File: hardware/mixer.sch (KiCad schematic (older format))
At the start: 31 parts, among them U26 5400BL15B050E, U27 5400BL15B050E, U28 5400BL15B050E, U29 ADL5802

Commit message: Current working version.
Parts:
- C107, C162: footprint fmcw3:C_0805b -> Capacitor_SMD:C_0805_2012Metric; symbol C -> Device:C
- C108, C115, C116, C117, C118, C119, C120, C121, C122, C123: footprint fmcw3:C_0402b -> Capacitor_SMD:C_0402_1005Metric; symbol C -> Device:C
- C109, C110, C111, C112, C113, C114: value 10p -> 3p; footprint fmcw3:C_0402b -> Capacitor_SMD:C_0402_1005Metric; symbol C -> Device:C
- F1, F2: symbol Via -> fmcw3-rescue:Via
- FB13: symbol FILTER -> Device:Ferrite_Bead
- R49, R50, R51, R52, R53, R54: symbol R -> Device:R
- U26, U27, U28: symbol 5400BL15B050E -> fmcw3-rescue:5400BL15B050E
- U29: footprint Housings_DFN_QFN:QFN-24-1EP_4x4mm_Pitch0.5mm -> Package_DFN_QFN:QFN-24-1EP_4x4mm_P0.5mm_EP2.6x2.6mm; symbol ADL5802 -> fmcw3-rescue:ADL5802; manf# (none) -> ADL5802ACPZ-R7
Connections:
- wire segments 91 -> 122

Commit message: Dropped the 3 from the end of the project name.
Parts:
- F1, F2: footprint fmcw3:RF_via -> fmcw:RF_via; symbol fmcw3-rescue:Via -> fmcw-rescue:Via-fmcw3-rescue
- FB13: footprint fmcw3:C_0603b -> fmcw:C_0603b
- R49, R50, R51, R52, R53, R54: footprint fmcw3:R_0402b -> fmcw:R_0402b
- U26, U27, U28: footprint fmcw3:5400BL15B050E -> fmcw:5400BL15B050E; symbol fmcw3-rescue:5400BL15B050E -> fmcw-rescue:5400BL15B050E-fmcw3-rescue
- U29: symbol fmcw3-rescue:ADL5802 -> fmcw-rescue:ADL5802-fmcw3-rescue
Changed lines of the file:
@@
 EESchema Schematic File Version 4
-LIBS:fmcw3-cache
+LIBS:fmcw-cache
 EELAYER 26 0
 EELAYER END
@@
 $EndComp
 $Comp
-L fmcw3-rescue:5400BL15B050E U?
+L fmcw-rescue:5400BL15B050E-fmcw3-rescue U?
 U 1 1 593ACD34
 P 2650 4550
@@
 F 0 "U26" H 2900 4800 60  0000 C CNN
 F 1 "5400BL15B050E" H 2750 5250 60  0000 C CNN
-F 2 "fmcw3:5400BL15B050E" H 2650 4550 60  0001 C CNN
-F 3 "https://www.johansontechnology.com/datasheets/baluns/Balun_5400BL15B050.pdf" H 2650 4550 60  0001 C CNN
+F 2 "fmcw:5400BL15B050E" H 2650 4550 60  0001 C CNN
+F 3 "https://www.johansontechnology.com/datasheets/5400BL15B050/5400BL15B050.pdf" H 2650 4550 60  0001 C CNN
 	1    2650 4550
 	1    0    0    -1
@@
 F 0 "R51" H 8330 3254 50  0000 R CNN
 F 1 "49.9" H 8330 3345 50  0000 R CNN
-F 2 "fmcw3:R_0402b" V 8330 3300 30  0001 C CNN
+F 2 "fmcw:R_0402b" V 8330 3300 30  0001 C CNN
 F 3 "" H 8400 3300 30  0000 C CNN
 	1    8400 3300
@@
 F 0 "R52" H 8330 3654 50  0000 R CNN
 F 1 "49.9" H 8330 3745 50  0000 R CNN
-F 2 "fmcw3:R_0402b" V 8330 3700 30  0001 C CNN
+F 2 "fmcw:R_0402b" V 8330 3700 30  0001 C CNN
 F 3 "" H 8400 3700 30  0000 C CNN
 	1    8400 3700
@@
 5V
 $Comp
-L fmcw3-rescue:ADL5802 U?
+L fmcw-rescue:ADL5802-fmcw3-rescue U?
 U 1 1 5942E974
 P 4650 4150
@@
 $EndComp
 $Comp
-L fmcw3-rescue:5400BL15B050E U27
+L fmcw-rescue:5400BL15B050E-fmcw3-rescue U27
 U 1 1 5942FD33
 P 2650 5500
@@
 F 0 "U27" H 2900 5750 60  0000 C CNN
 F 1 "5400BL15B050E" H 2750 6200 60  0000 C CNN
-F 2 "fmcw3:5400BL15B050E" H 2650 5500 60  0001 C CNN
+F 2 "fmcw:5400BL15B050E" H 2650 5500 60  0001 C CNN
 F 3 "" H 2650 5500 60  0000 C CNN
 	1    2650 5500
@@
 RF1
 $Comp
-L fmcw3-rescue:5400BL15B050E U28
+L fmcw-rescue:5400BL15B050E-fmcw3-rescue U28
 U 1 1 59430048
 P 2650 6500
@@
 F 0 "U28" H 2900 6750 60  0000 C CNN
 F 1 "5400BL15B050E" H 2750 7200 60  0000 C CNN
-F 2 "fmcw3:5400BL15B050E" H 2650 6500 60  0001 C CNN
+F 2 "fmcw:5400BL15B050E" H 2650 6500 60  0001 C CNN
 F 3 "" H 2650 6500 60  0000 C CNN
 	1    2650 6500
@@
 F 0 "R53" H 8330 4854 50  0000 R CNN
 F 1 "49.9" H 8330 4945 50  0000 R CNN
-F 2 "fmcw3:R_0402b" V 8330 4900 30  0001 C CNN
+F 2 "fmcw:R_0402b" V 8330 4900 30  0001 C CNN
 F 3 "" H 8400 4900 30  0000 C CNN
 	1    8400 4900
@@
 F 0 "R54" H 8330 5254 50  0000 R CNN
 F 1 "49.9" H 8330 5345 50  0000 R CNN
-F 2 "fmcw3:R_0402b" V 8330 5300 30  0001 C CNN
+F 2 "fmcw:R_0402b" V 8330 5300 30  0001 C CNN
 F 3 "" H 8400 5300 30  0000 C CNN
 	1    8400 5300
@@
 F 0 "R50" V 7030 5350 50  0000 C CNN
 F 1 "DNP" V 6950 5350 50  0000 C CNN
-F 2 "fmcw3:R_0402b" V 6880 5350 30  0001 C CNN
+F 2 "fmcw:R_0402b" V 6880 5350 30  0001 C CNN
 F 3 "" H 6950 5350 30  0000 C CNN
 	1    6950 5350
@@
 F 0 "R49" V 7030 4950 50  0000 C CNN
 F 1 "2k" V 6950 4950 50  0000 C CNN
-F 2 "fmcw3:R_0402b" V 6880 4950 30  0001 C CNN
+F 2 "fmcw:R_0402b" V 6880 4950 30  0001 C CNN
 F 3 "" H 6950 4950 30  0000 C CNN
 	1    6950 4950
@@
 F 0 "FB13" V 3600 2050 50  0000 C CNN
 F 1 "BLM18PG181SN1D" V 3500 2200 50  0000 C CNN
-F 2 "fmcw3:C_0603b" H 3650 2200 60  0001 C CNN
+F 2 "fmcw:C_0603b" H 3650 2200 60  0001 C CNN
 F 3 "" H 3650 2200 60  0000 C CNN
 	1    3650 2200
@@
 Connection ~ 5700 2450
 $Comp
-L fmcw3-rescue:Via F1
+L fmcw-rescue:Via-fmcw3-rescue F1
 U 1 1 597038AD
 P 1150 4050
 F 0 "F1" H 1068 4297 60  0000 C CNN
 F 1 "Via" H 1068 4191 60  0000 C CNN
-F 2 "fmcw3:RF_via" H 1150 4050 60  0001 C CNN
+F 2 "fmcw:RF_via" H 1150 4050 60  0001 C CNN
 F 3 "" H 1150 4050 60  0001 C CNN
 	1    1150 4050
@@
 $EndComp
 $Comp
-L fmcw3-rescue:Via F2
+L fmcw-rescue:Via-fmcw3-rescue F2
 U 1 1 5970394E
 P 1900 4050
 F 0 "F2" H 1819 4297 60  0000 C CNN
 F 1 "Via" H 1819 4191 60  0000 C CNN
-F 2 "fmcw3:RF_via" H 1900 4050 60  0001 C CNN
+F 2 "fmcw:RF_via" H 1900 4050 60  0001 C CNN
 F 3 "" H 1900 4050 60  0001 C CNN
 	1    1900 4050

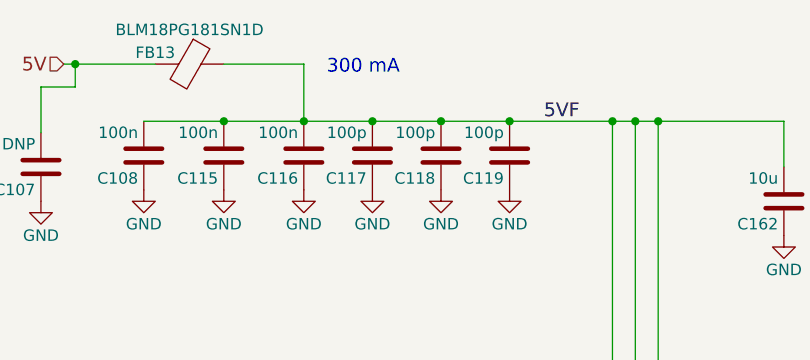
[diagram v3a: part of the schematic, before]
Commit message: Adjusted power supply for new power amplifier.
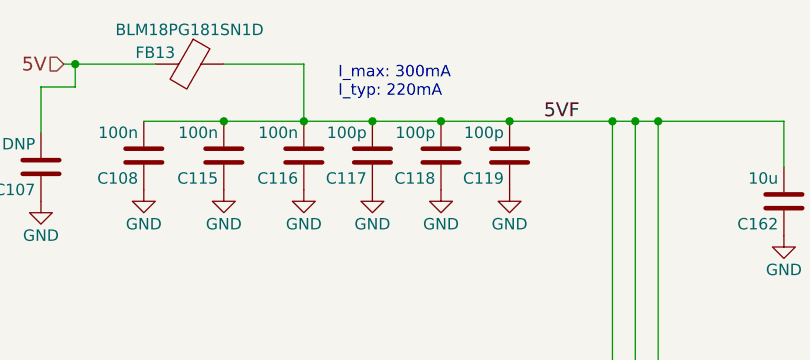
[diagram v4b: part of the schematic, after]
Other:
- note added: "I_max: 300mA\nI_typ: 220mA"
- note removed: "300 mA"
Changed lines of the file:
@@
 EESchema Schematic File Version 4
 LIBS:fmcw-cache
-EELAYER 29 0
+EELAYER 26 0
 EELAYER END
 $Descr A4 11693 8268
@@
 Text Label 6950 4750 0    60   ~ 0
 5VF
-Text Notes 4250 2250 0    60   ~ 0
-300 mA
+Text Notes 4300 2350 0    50   ~ 0
+I_max: 300mA\nI_typ: 220mA
 $Comp
 L Device:Ferrite_Bead FB13

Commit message: Documentation for TPS5420D buck converter.
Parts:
- C162: MFN (none) -> 885012107014
- U29: MFN (none) -> ADL5802ACPZ-R7; manf# ADL5802ACPZ-R7 -> (none)
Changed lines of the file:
@@
 F 2 "Package_DFN_QFN:QFN-24-1EP_4x4mm_P0.5mm_EP2.6x2.6mm" H 4650 4150 60  0001 C CNN
 F 3 "http://www.analog.com/media/en/technical-documentation/data-sheets/ADL5802.pdf" H 4650 4150 60  0001 C CNN
-F 4 "ADL5802ACPZ-R7" H 4650 4150 50  0001 C CNN "manf#"
+F 4 "" H 4650 4150 50  0001 C CNN "manf#"
+F 5 "ADL5802ACPZ-R7" H 0   0   50  0001 C CNN "MFN"
 	1    4650 4150
 	1    0    0    -1
@@
 F 2 "Capacitor_SMD:C_0805_2012Metric" H 6288 2650 30  0001 C CNN
 F 3 "" H 6250 2800 60  0000 C CNN
+F 4 "885012107014" H 0   0   50  0001 C CNN "MFN"
 	1    6250 2800
 	-1   0    0    1

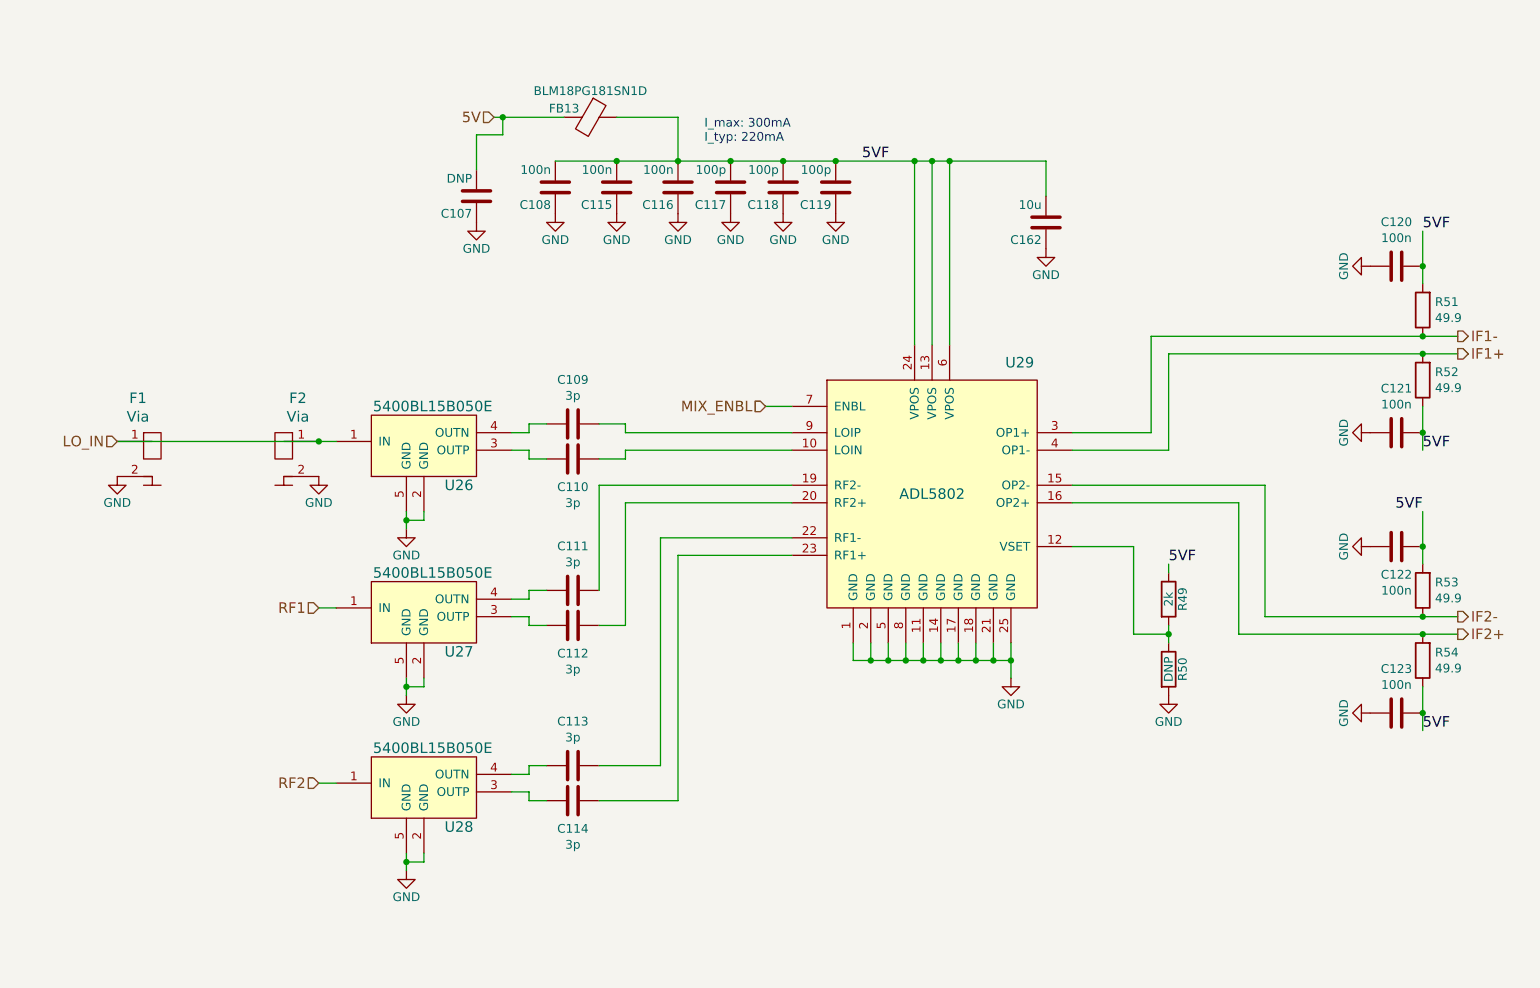
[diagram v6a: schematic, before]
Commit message: Added MFNs to components.
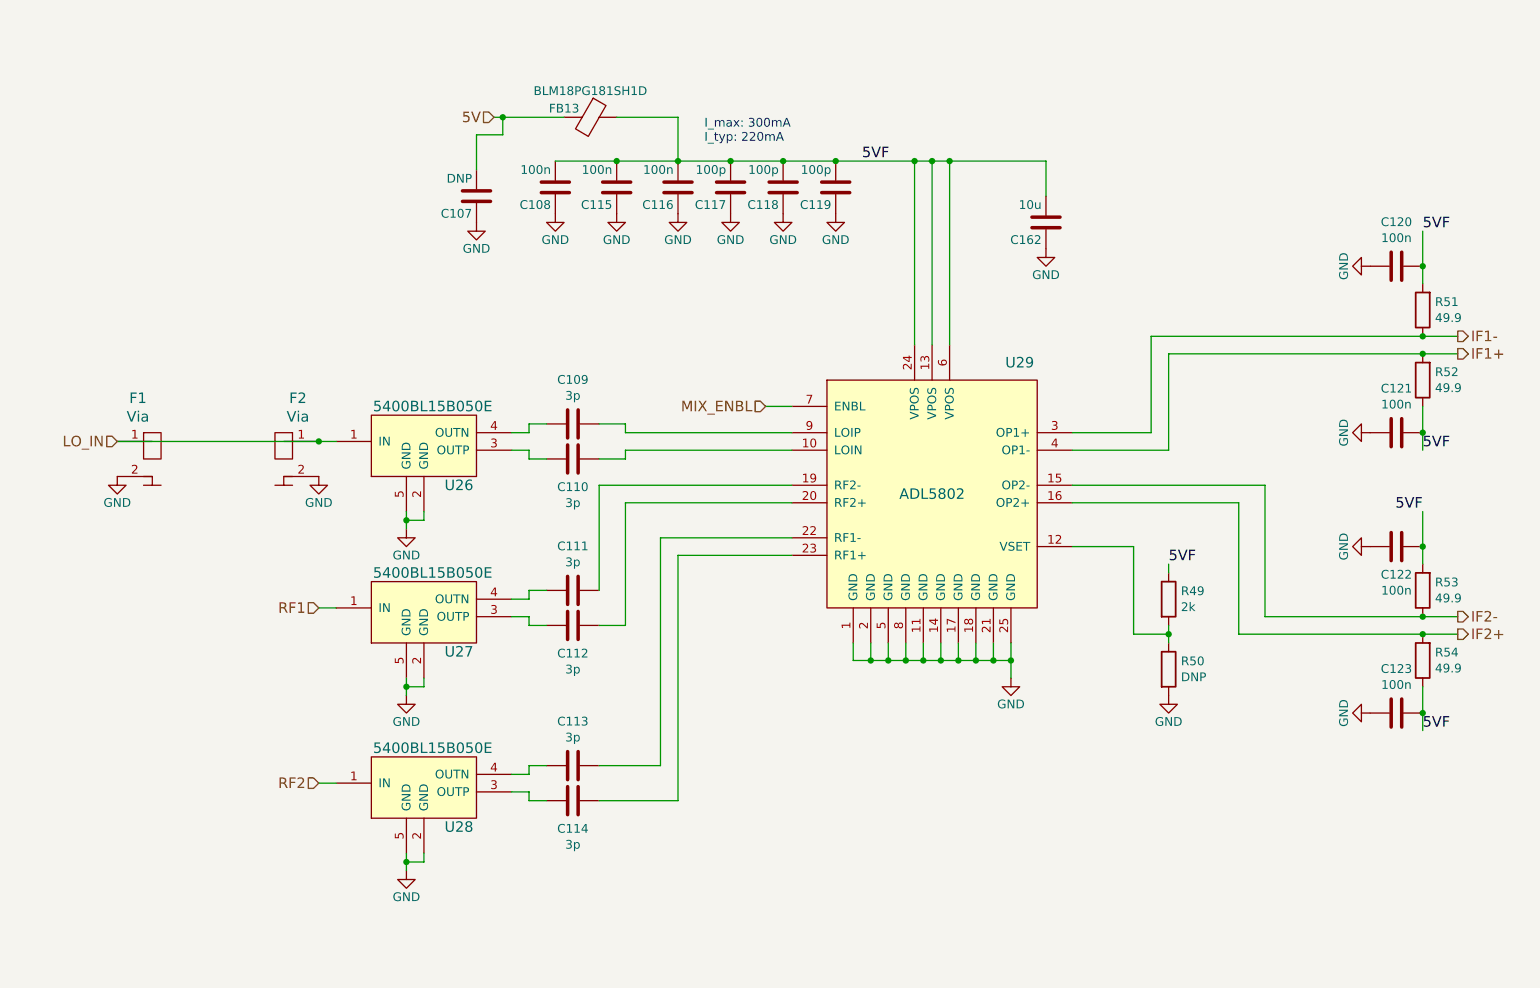
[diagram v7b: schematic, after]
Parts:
- C108, C115, C116, C120, C121, C122, C123: MFN (none) -> CL05B104KO5NNNC
- C109, C110, C111, C112, C113, C114: MFN (none) -> 500R07S3R0BV4T
- C117, C118, C119: MFN (none) -> UMK105CG101JVHF
- C162: MFN 885012107014 -> CL21B106KQQNNNE
- FB13: value BLM18PG181SN1D -> BLM18PG181SH1D; footprint fmcw:C_0603b -> Inductor_SMD:L_0603_1608Metric; MFN (none) -> BLM18PG181SH1D
- R49: footprint fmcw:R_0402b -> Resistor_SMD:R_0402_1005Metric; MFN (none) -> ERJ-2RKF2001X
- R50: footprint fmcw:R_0402b -> Resistor_SMD:R_0402_1005Metric
- R51, R52, R53, R54: footprint fmcw:R_0402b -> Resistor_SMD:R_0402_1005Metric; MFN (none) -> ERJ-2RKF49R9X
- U26, U27, U28: MFN (none) -> 5400BL15B050E
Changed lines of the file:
@@
 F 2 "fmcw:5400BL15B050E" H 2650 4550 60  0001 C CNN
 F 3 "https://www.johansontechnology.com/datasheets/5400BL15B050/5400BL15B050.pdf" H 2650 4550 60  0001 C CNN
+F 4 "5400BL15B050E" H 0   0   50  0001 C CNN "MFN"
 	1    2650 4550
 	1    0    0    -1
@@
 F 2 "Capacitor_SMD:C_0402_1005Metric" H 3588 3800 30  0001 C CNN
 F 3 "" H 3550 3950 60  0000 C CNN
+F 4 " 500R07S3R0BV4T" H 0   0   50  0001 C CNN "MFN"
 	1    3550 3950
 	0    1    1    0
@@
 F 2 "Capacitor_SMD:C_0402_1005Metric" H 3588 4000 30  0001 C CNN
 F 3 "" H 3550 4150 60  0000 C CNN
+F 4 " 500R07S3R0BV4T" H 0   0   50  0001 C CNN "MFN"
 	1    3550 4150
 	0    1    1    0
@@
 F 2 "Capacitor_SMD:C_0402_1005Metric" H 4488 2450 30  0001 C CNN
 F 3 "" H 4450 2600 60  0000 C CNN
+F 4 "UMK105CG101JVHF" H 0   0   50  0001 C CNN "MFN"
 	1    4450 2600
 	-1   0    0    1
@@
 F 2 "Capacitor_SMD:C_0402_1005Metric" H 4188 2450 30  0001 C CNN
 F 3 "" H 4150 2600 60  0000 C CNN
+F 4 "CL05B104KO5NNNC" H 0   0   50  0001 C CNN "MFN"
 	1    4150 2600
 	-1   0    0    1
@@
 F 0 "R51" H 8330 3254 50  0000 R CNN
 F 1 "49.9" H 8330 3345 50  0000 R CNN
-F 2 "fmcw:R_0402b" V 8330 3300 30  0001 C CNN
+F 2 "Resistor_SMD:R_0402_1005Metric" V 8330 3300 30  0001 C CNN
 F 3 "" H 8400 3300 30  0000 C CNN
+F 4 "ERJ-2RKF49R9X" H 0   0   50  0001 C CNN "MFN"
 	1    8400 3300
 	-1   0    0    1
@@
 F 0 "R52" H 8330 3654 50  0000 R CNN
 F 1 "49.9" H 8330 3745 50  0000 R CNN
-F 2 "fmcw:R_0402b" V 8330 3700 30  0001 C CNN
+F 2 "Resistor_SMD:R_0402_1005Metric" V 8330 3700 30  0001 C CNN
 F 3 "" H 8400 3700 30  0000 C CNN
+F 4 "ERJ-2RKF49R9X" H 0   0   50  0001 C CNN "MFN"
 	1    8400 3700
 	-1   0    0    1
@@
 F 2 "Capacitor_SMD:C_0402_1005Metric" H 8288 2900 30  0001 C CNN
 F 3 "" H 8250 3050 60  0000 C CNN
+F 4 "CL05B104KO5NNNC" H 0   0   50  0001 C CNN "MFN"
 	1    8250 3050
 	0    -1   -1   0
@@
 F 2 "Capacitor_SMD:C_0402_1005Metric" H 8288 3850 30  0001 C CNN
 F 3 "" H 8250 4000 60  0000 C CNN
+F 4 "CL05B104KO5NNNC" H 0   0   50  0001 C CNN "MFN"
 	1    8250 4000
 	0    -1   -1   0
@@
 F 2 "fmcw:5400BL15B050E" H 2650 5500 60  0001 C CNN
 F 3 "" H 2650 5500 60  0000 C CNN
+F 4 "5400BL15B050E" H 0   0   50  0001 C CNN "MFN"
 	1    2650 5500
 	1    0    0    -1
@@
 F 2 "Capacitor_SMD:C_0402_1005Metric" H 3588 4750 30  0001 C CNN
 F 3 "" H 3550 4900 60  0000 C CNN
+F 4 " 500R07S3R0BV4T" H 0   0   50  0001 C CNN "MFN"
 	1    3550 4900
 	0    1    1    0
@@
 F 2 "Capacitor_SMD:C_0402_1005Metric" H 3588 4950 30  0001 C CNN
 F 3 "" H 3550 5100 60  0000 C CNN
+F 4 " 500R07S3R0BV4T" H 0   0   50  0001 C CNN "MFN"
 	1    3550 5100
 	0    1    1    0
@@
 F 2 "fmcw:5400BL15B050E" H 2650 6500 60  0001 C CNN
 F 3 "" H 2650 6500 60  0000 C CNN
+F 4 "5400BL15B050E" H 0   0   50  0001 C CNN "MFN"
 	1    2650 6500
 	1    0    0    -1
@@
 F 2 "Capacitor_SMD:C_0402_1005Metric" H 3588 5750 30  0001 C CNN
 F 3 "" H 3550 5900 60  0000 C CNN
+F 4 " 500R07S3R0BV4T" H 0   0   50  0001 C CNN "MFN"
 	1    3550 5900
 	0    1    1    0
@@
 F 2 "Capacitor_SMD:C_0402_1005Metric" H 3588 5950 30  0001 C CNN
 F 3 "" H 3550 6100 60  0000 C CNN
+F 4 " 500R07S3R0BV4T" H 0   0   50  0001 C CNN "MFN"
 	1    3550 6100
 	0    1    1    0
@@
 F 0 "R53" H 8330 4854 50  0000 R CNN
 F 1 "49.9" H 8330 4945 50  0000 R CNN
-F 2 "fmcw:R_0402b" V 8330 4900 30  0001 C CNN
+F 2 "Resistor_SMD:R_0402_1005Metric" V 8330 4900 30  0001 C CNN
 F 3 "" H 8400 4900 30  0000 C CNN
+F 4 "ERJ-2RKF49R9X" H 0   0   50  0001 C CNN "MFN"
 	1    8400 4900
 	-1   0    0    1
@@
 F 0 "R54" H 8330 5254 50  0000 R CNN
 F 1 "49.9" H 8330 5345 50  0000 R CNN
-F 2 "fmcw:R_0402b" V 8330 5300 30  0001 C CNN
+F 2 "Resistor_SMD:R_0402_1005Metric" V 8330 5300 30  0001 C CNN
 F 3 "" H 8400 5300 30  0000 C CNN
+F 4 "ERJ-2RKF49R9X" H 0   0   50  0001 C CNN "MFN"
 	1    8400 5300
 	-1   0    0    1
@@
 F 2 "Capacitor_SMD:C_0402_1005Metric" H 8288 4500 30  0001 C CNN
 F 3 "" H 8250 4650 60  0000 C CNN
+F 4 "CL05B104KO5NNNC" H 0   0   50  0001 C CNN "MFN"
 	1    8250 4650
 	0    -1   -1   0
@@
 F 2 "Capacitor_SMD:C_0402_1005Metric" H 8288 5450 30  0001 C CNN
 F 3 "" H 8250 5600 60  0000 C CNN
+F 4 "CL05B104KO5NNNC" H 0   0   50  0001 C CNN "MFN"
 	1    8250 5600
 	0    -1   -1   0
@@
 F 2 "Capacitor_SMD:C_0402_1005Metric" H 4788 2450 30  0001 C CNN
 F 3 "" H 4750 2600 60  0000 C CNN
+F 4 "UMK105CG101JVHF" H 0   0   50  0001 C CNN "MFN"
 	1    4750 2600
 	-1   0    0    1
@@
 F 2 "Capacitor_SMD:C_0402_1005Metric" H 5088 2450 30  0001 C CNN
 F 3 "" H 5050 2600 60  0000 C CNN
+F 4 "UMK105CG101JVHF" H 0   0   50  0001 C CNN "MFN"
 	1    5050 2600
 	-1   0    0    1
@@
 F 2 "Capacitor_SMD:C_0402_1005Metric" H 3838 2450 30  0001 C CNN
 F 3 "" H 3800 2600 60  0000 C CNN
+F 4 "CL05B104KO5NNNC" H 0   0   50  0001 C CNN "MFN"
 	1    3800 2600
 	-1   0    0    1
@@
 F 2 "Capacitor_SMD:C_0402_1005Metric" H 3488 2450 30  0001 C CNN
 F 3 "" H 3450 2600 60  0000 C CNN
+F 4 "CL05B104KO5NNNC" H 0   0   50  0001 C CNN "MFN"
 	1    3450 2600
 	-1   0    0    1
@@
 AR Path="/59396B97/593ABC4F/594321EF" Ref="R?"  Part="1"
 AR Path="/59434BD2/594321EF" Ref="R50"  Part="1"
-F 0 "R50" V 7030 5350 50  0000 C CNN
-F 1 "DNP" V 6950 5350 50  0000 C CNN
-F 2 "fmcw:R_0402b" V 6880 5350 30  0001 C CNN
+F 0 "R50" H 7020 5396 50  0000 L CNN
+F 1 "DNP" H 7020 5305 50  0000 L CNN
+F 2 "Resistor_SMD:R_0402_1005Metric" V 6880 5350 30  0001 C CNN
 F 3 "" H 6950 5350 30  0000 C CNN
 	1    6950 5350
@@
 U 1 1 594327C4
 P 6950 4950
-F 0 "R49" V 7030 4950 50  0000 C CNN
-F 1 "2k" V 6950 4950 50  0000 C CNN
-F 2 "fmcw:R_0402b" V 6880 4950 30  0001 C CNN
+F 0 "R49" H 7020 4996 50  0000 L CNN
+F 1 "2k" H 7020 4905 50  0000 L CNN
+F 2 "Resistor_SMD:R_0402_1005Metric" V 6880 4950 30  0001 C CNN
 F 3 "" H 6950 4950 30  0000 C CNN
+F 4 "ERJ-2RKF2001X" H 0   0   50  0001 C CNN "MFN"
 	1    6950 4950
 	1    0    0    -1
@@
 P 3650 2200
 F 0 "FB13" V 3600 2050 50  0000 C CNN
-F 1 "BLM18PG181SN1D" V 3500 2200 50  0000 C CNN
-F 2 "fmcw:C_0603b" H 3650 2200 60  0001 C CNN
+F 1 "BLM18PG181SH1D" V 3500 2200 50  0000 C CNN
+F 2 "Inductor_SMD:L_0603_1608Metric" H 3650 2200 60  0001 C CNN
 F 3 "" H 3650 2200 60  0000 C CNN
+F 4 "BLM18PG181SH1D" H 0   0   50  0001 C CNN "MFN"
 	1    3650 2200
 	0    1    1    0
@@
 F 2 "Capacitor_SMD:C_0805_2012Metric" H 6288 2650 30  0001 C CNN
 F 3 "" H 6250 2800 60  0000 C CNN
-F 4 "885012107014" H 0   0   50  0001 C CNN "MFN"
+F 4 "CL21B106KQQNNNE" H 0   0   50  0001 C CNN "MFN"
 	1    6250 2800
 	-1   0    0    1
